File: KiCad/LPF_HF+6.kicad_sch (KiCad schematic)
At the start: 129 parts, among them J1 Conn_01x07, J2 12V INPUT, J3 RF input, J4 Conn_01x07, J5 RF output, U1 AMS1117-5, U2 74AHC595, U3 ULN2003

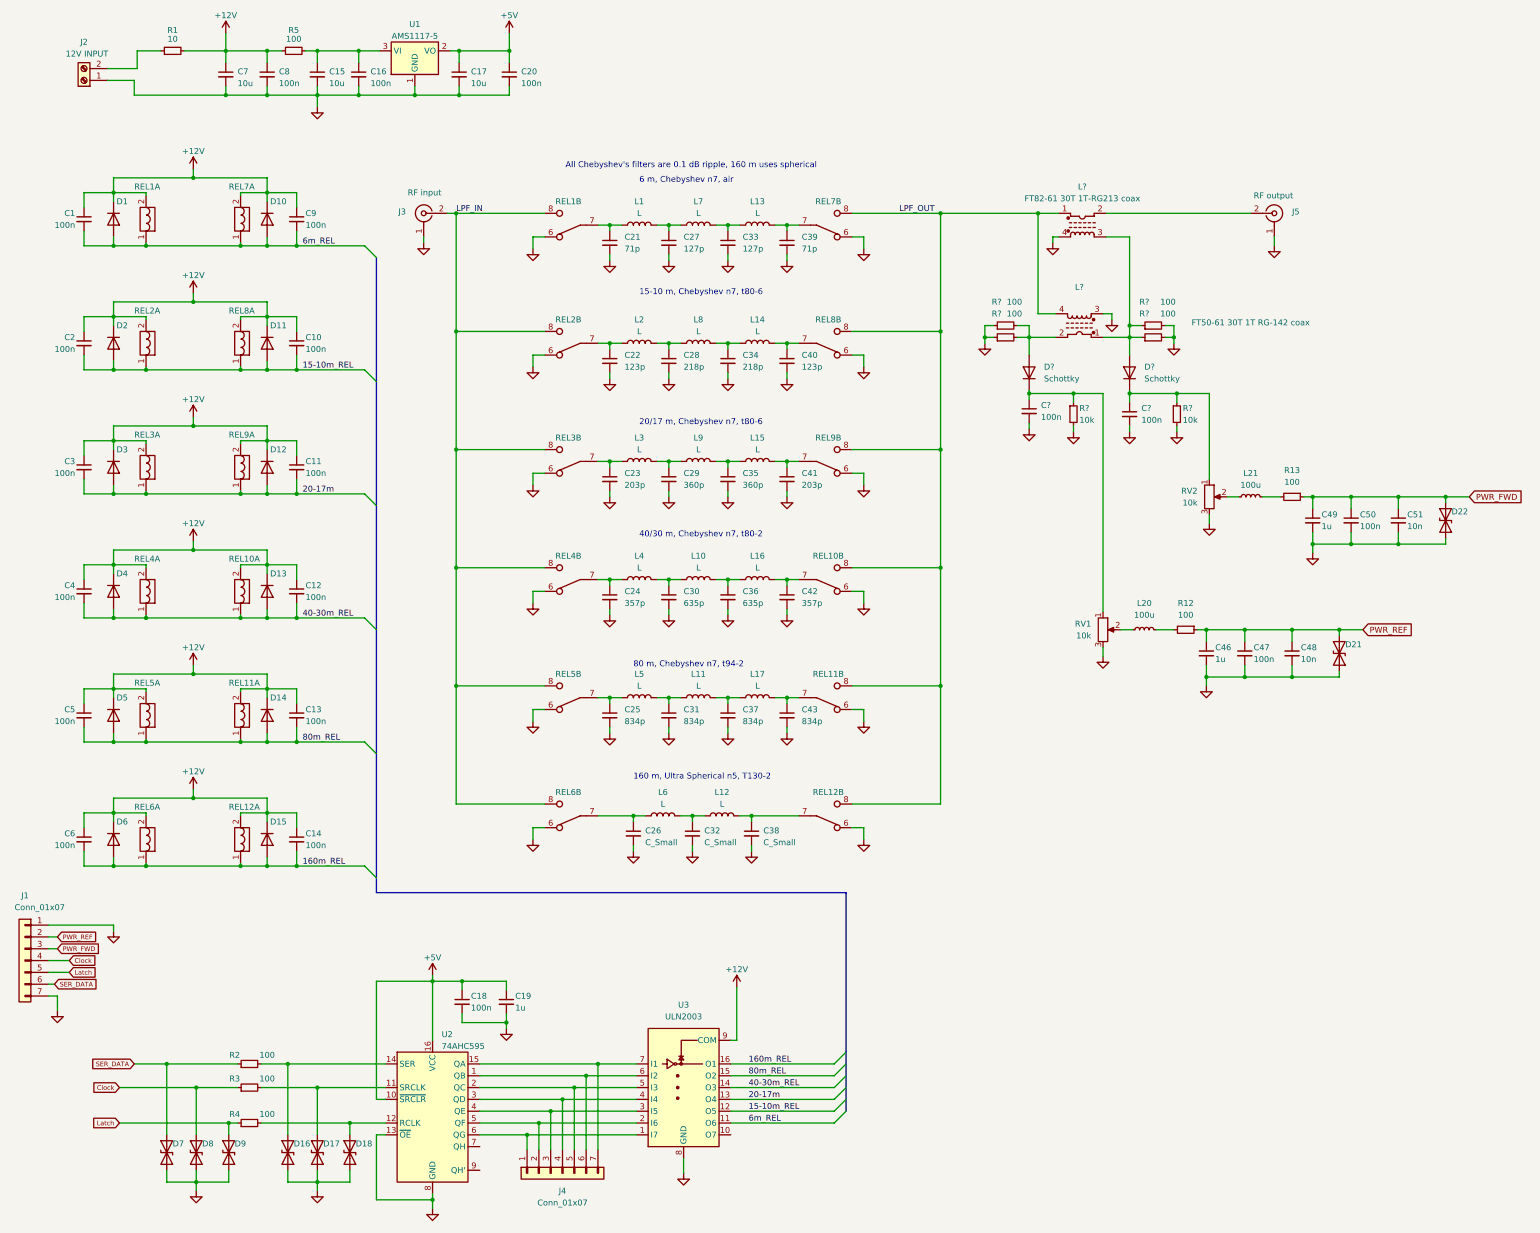
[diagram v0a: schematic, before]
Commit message: ERC DRC run and show no significant issues
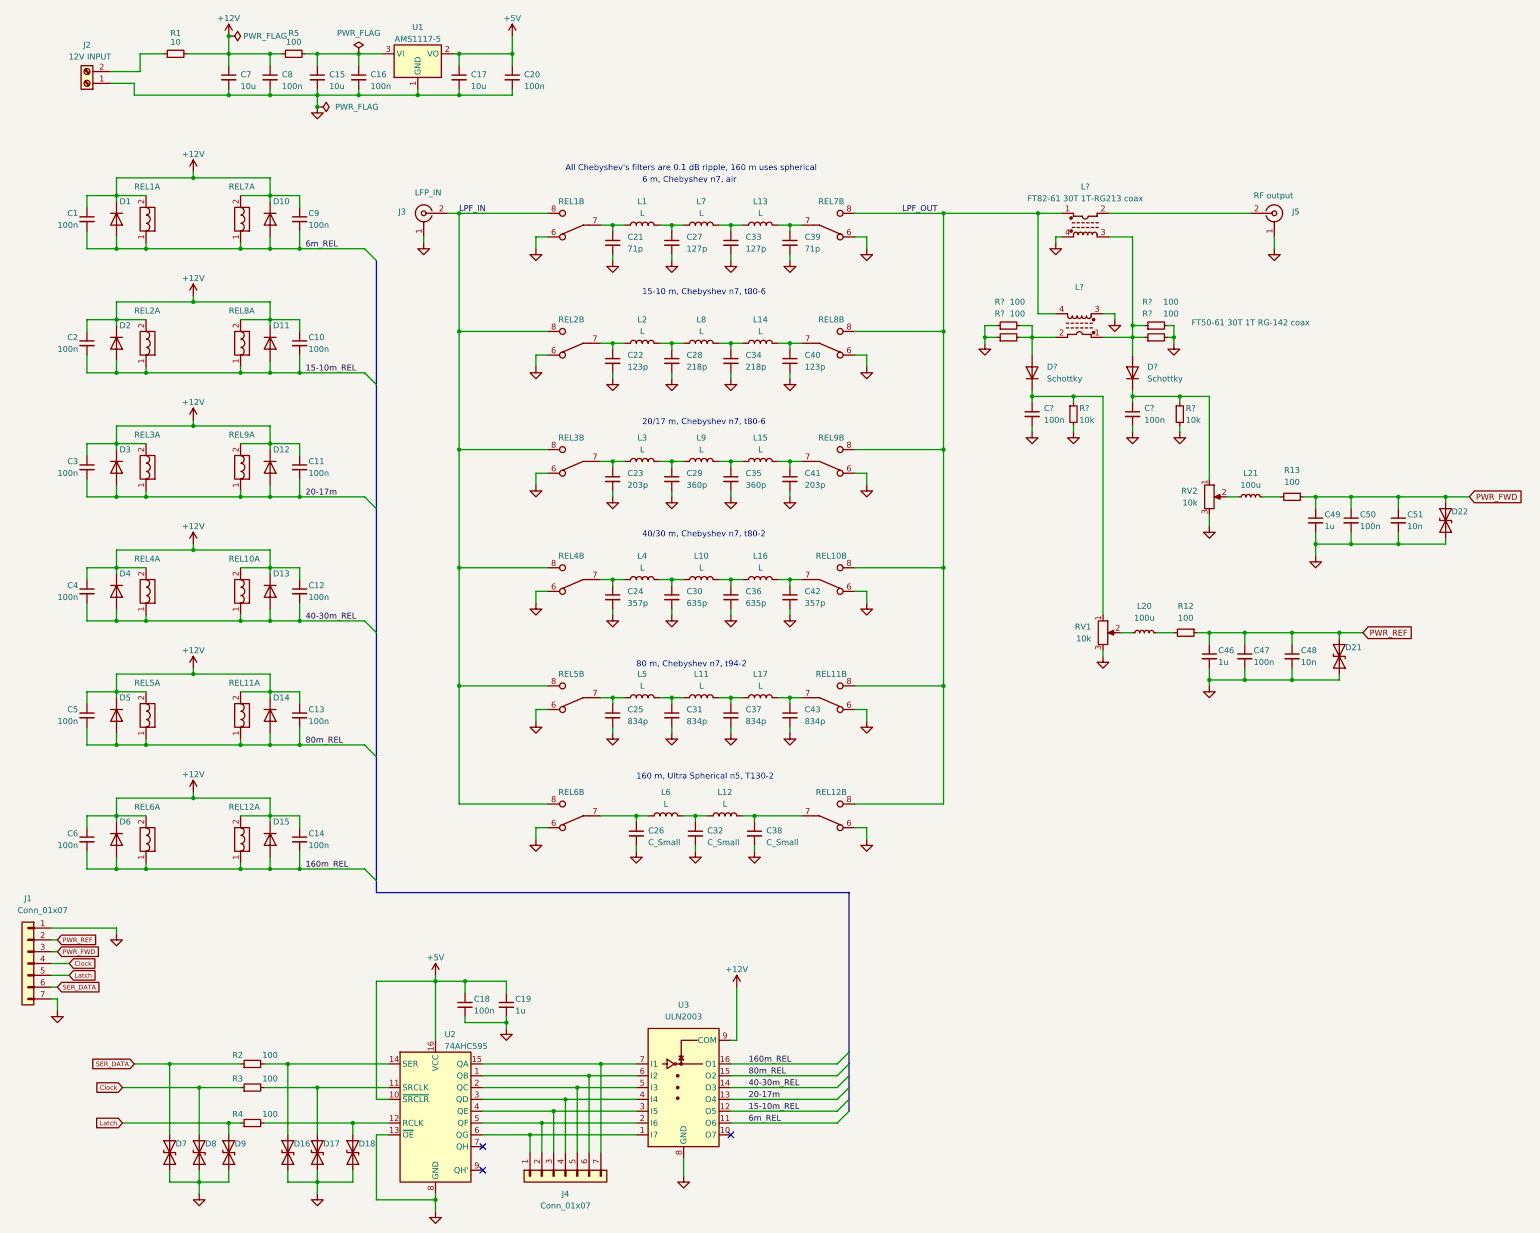
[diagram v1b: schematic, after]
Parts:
- J3: value RF input -> LFP_IN
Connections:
- no-connect marks 0 -> 3
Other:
- moved on the sheet: C1, C10, C11, C12, C13, C14, C15, C16, C17, C18, C19, C2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
